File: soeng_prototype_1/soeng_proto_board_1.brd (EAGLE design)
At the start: 86.3 x 37.8 mm, 17 parts, among them J1 2172034-1, T1 2N2222

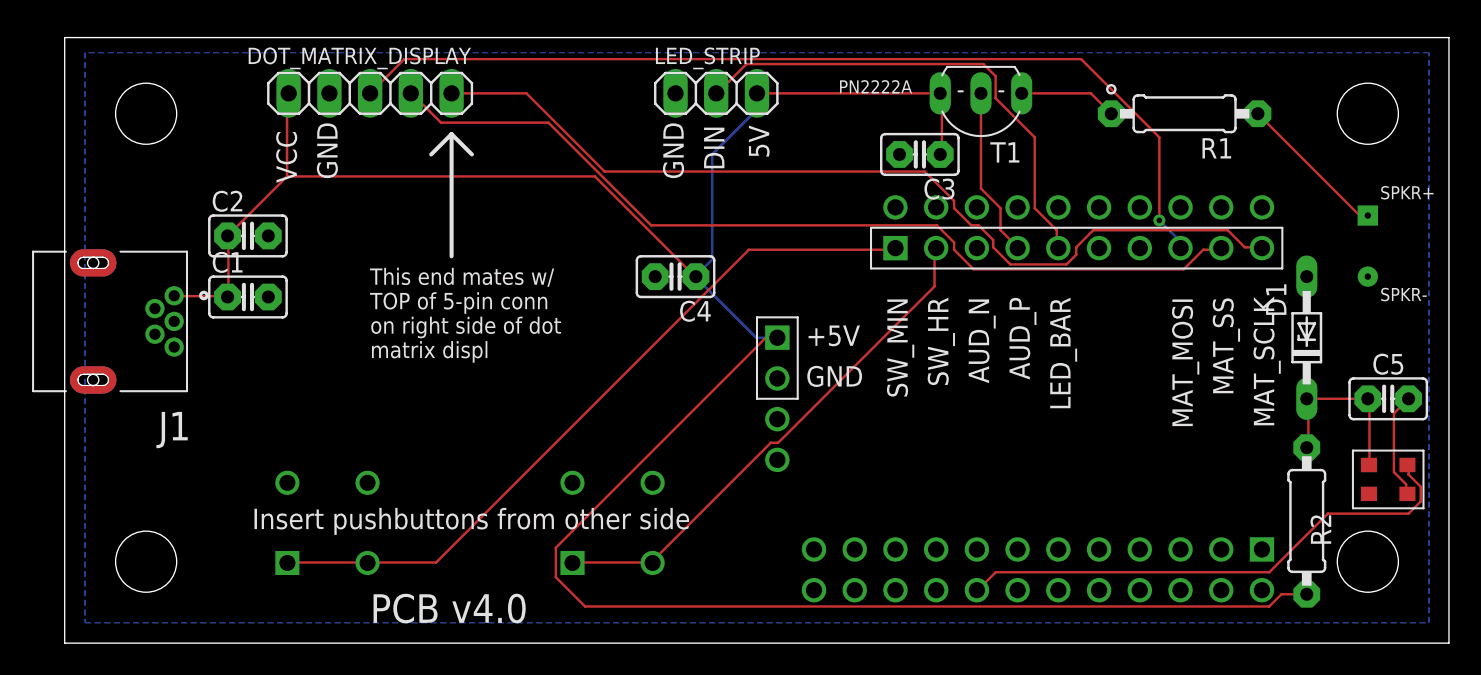
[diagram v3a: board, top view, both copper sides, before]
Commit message: Added TCXO, 3.3V Zener, RC
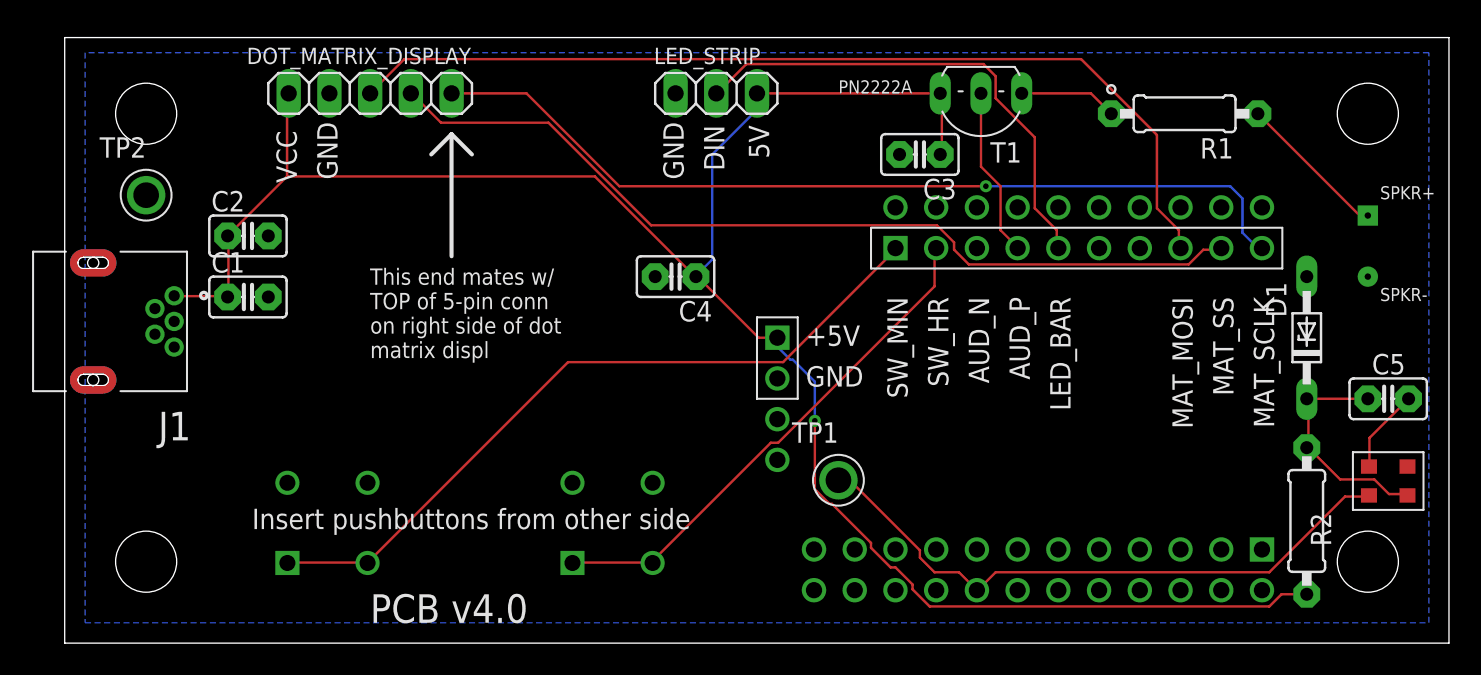
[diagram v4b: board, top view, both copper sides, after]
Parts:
- added TP1, TP2: 5010, 5010:TP_5010
- turned U$5 to 180 degrees
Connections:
- net GND: now also TP2.1
- net N$10: now also TP1.1
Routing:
- net +5V: track 150.1 -> 125.9 mm, vias 0 -> 1
- net N$10: track 32.6 -> 38.6 mm
- net N$11: track 11.2 -> 14.4 mm
- net GND: track 6.65 -> 5.24 mm
- net N$1: track 57.1 -> 55.8 mm, vias 0 -> 1
- net N$3: vias 1 -> 0

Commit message: V4.1 sent out for fab.  Changed oscillator, added level shifters
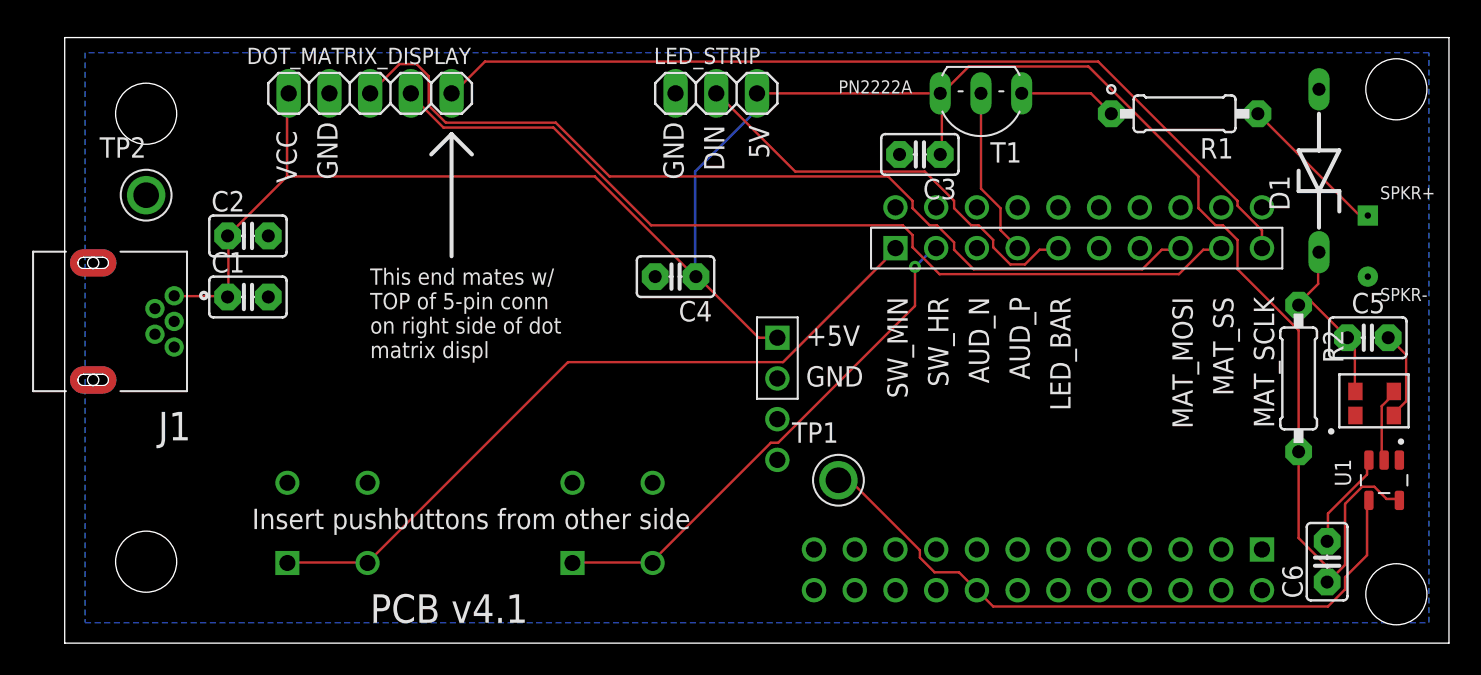
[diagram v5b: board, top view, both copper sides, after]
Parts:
- added C6: (no value), adafruit:C025-025X050
- added U1: SN74LV1T34DBVR, SN74LV1T34DBVR:SOT95P280X145-5N
- D1: device diode:DO34Z7 -> diode:ZDIO-10
- U$5: value TXEAPLSANF -> ILSI-I538; device lap_2019:TXEAPLSANF -> lap_2019:ILSI-I538SERIES
- moved D1 10.4 mm to (78.2, 29.5)
- moved R2 8.90 mm to (77.0, 16.5)
- moved C5 4.02 mm to (81.3, 19.1)
- moved U$5 3.97 mm to (79.5, 12.7), turned to 0 degrees
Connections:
- new net 3V3: C5.1, D1.C, R2.1, U$5.ILSI4
- net +5V: now also C6.1, U1.5
- net GND: now also C6.2, U$5.ILSI2, U1.3; no longer U$5.TCXO2
- net N$10: now also U1.4; no longer U$5.TCXO3
- net N$11: now also U$5.ILSI3, U1.2; no longer C5.1, D1.C, R2.1, U$5.TCXO4
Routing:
- net +5V: track 125.9 -> 139.5 mm, vias 1 -> 0
- net 3V3: track 0.00 -> 11.8 mm
- net N$11: track 14.4 -> 4.75 mm
- net GND: track 5.24 -> 11.8 mm
- net N$5: track 30.9 -> 26.7 mm
- net N$10: track 38.6 -> 41.8 mm
- net N$1: track 55.8 -> 57.0 mm, vias 1 -> 0
- net N$2: track 55.7 -> 56.6 mm
- net N$3: track 59.6 -> 58.8 mm
- net N$7: vias 0 -> 1
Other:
- board text added: "PCB v4.1"
- board text removed: "PCB v4.0"
